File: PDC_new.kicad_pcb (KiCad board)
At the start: 2 copper layers, 156.5 x 145.5 mm, 83 parts, among them J1 Conn_01x02_Pin, J10 Conn_01x02_Pin, J11 XT90PW(2+2)-M.G.Y, J12 Conn_01x02_Pin, J13 Conn_01x02_Pin, J14 Conn_01x02_Pin, J15 Conn_01x02_Pin, J2 Conn_01x02_Pin, J3 Conn_01x02_Pin, J4 Conn_01x02_Pin, J5 Conn_01x02_Pin, J6 Conn_01x02_Pin, J7 Conn_01x02_Pin, J8 Conn_01x02_Pin, J9 Conn_01x02_Pin, Q2 IRF540NSTRLPBF, U1 TPSI3050QDWZRQ1, U10 LM393LVDR, U11 IPB017N10N5ATMA1, U12 IPB017N10N5ATMA1, U14 IPB017N10N5ATMA1, U2 TPSI3050QDWZRQ1, U4 74HC74, U5 URB4805LD-60WR3, U6 IPB017N10N5ATMA1, U7 TLC555CDR, U8 SN74HC08D, U9 SN74HC14DR

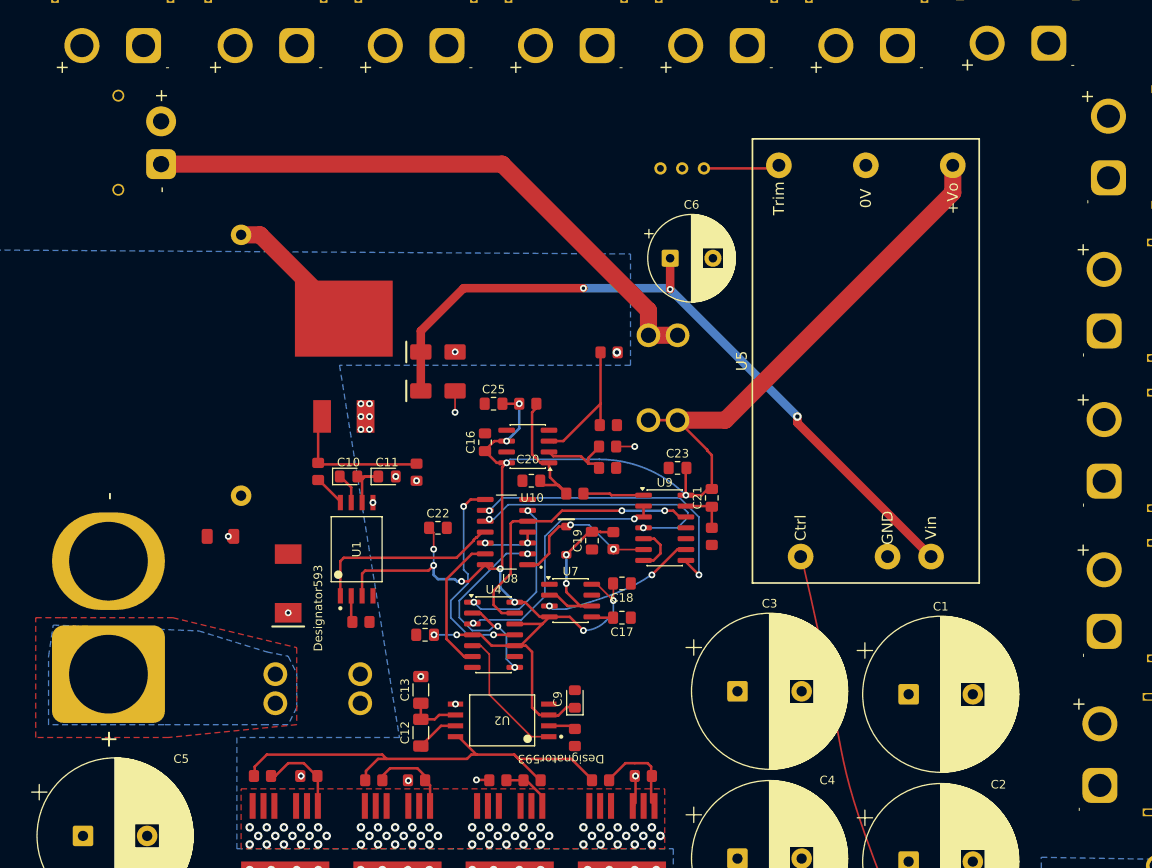
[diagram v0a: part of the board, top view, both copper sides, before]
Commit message: Final touchup, solved vias issues and XT30 connector mismatch
Co-Authored-By: Claude Opus 5.5 <noreply@anthropic.com>
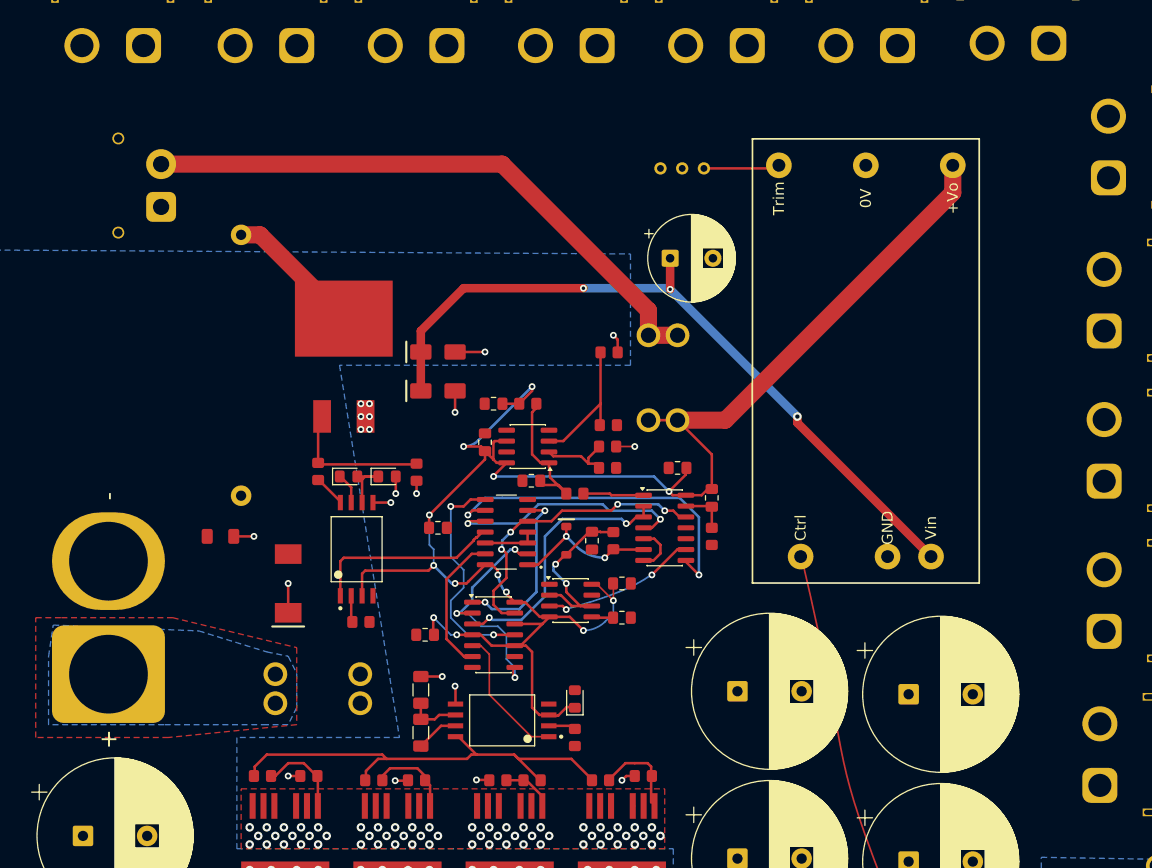
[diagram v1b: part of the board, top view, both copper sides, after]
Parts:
- moved J12 5.00 mm to (258.1, 163.5)
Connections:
- F4 pad 1: Net-(J12-Pin_1) -> Net-(J12-Pin_2)
- J12 pad 1: Net-(J12-Pin_1) -> GND
- J12 pad 2: GND -> Net-(J12-Pin_2)
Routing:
- net Net-(J12-Pin_2): track 0.00 -> 70.3 mm
- net Net-(J12-Pin_1): track 70.3 -> 0.00 mm
- net /+5V: track 198.6 -> 216.7 mm
- net /BUS+: track 11.8 -> 23.5 mm
- net /BATT+: track 1.21 -> 11.5 mm
- net /TIMEOUT: track 35.6 -> 40.1 mm
- net /DONE_N: track 31.2 -> 28.7 mm
- net /RUN_CLR_N: track 18.6 -> 20.6 mm
- net /FAULT_SET: track 25.2 -> 26.9 mm
- net /TIMER_RC: track 21.7 -> 23.0 mm
- net /MSTR_ON: track 18.3 -> 17.3 mm
- net GND: track 6.28 -> 5.59 mm
- net /PC_DONE: track 30.5 -> 31.2 mm
- net /reset_N: track 34.6 -> 35.2 mm, vias 2 -> 4
- net /FAULT_N: track 27.1 -> 27.6 mm
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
